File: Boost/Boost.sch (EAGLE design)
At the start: 2 parts

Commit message: boost
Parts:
- added C1: 10nF, adafruit:CPOL-USE2.5-5
- added C2, C4, C5, C6: 22uF, adafruit:CPOL-USE2.5-5
- added JP1: (no value), adafruit:PINHD-1X3
- added JP2: M02PTH, SparkFun-Connectors:M02PTH
- added L1: 1uH, eagle-ltspice:L0207/10
- added R3: 1M Ohm, adafruit:R-US_0207/10
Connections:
- new net N$1: C1.-, C4.-, C6.-, JP1.1, JP2.2, TPS61230.GND
- new net N$10: C2.-, C5.+
- new net N$2: R3.1, TPS61230.PG
- new net N$3: L1.2, TPS61230.SW1, TPS61230.SW2
- new net N$4: C2.+, JP1.3, R3.2, TPS61230.VOUT1, TPS61230.VOUT2
- new net N$5: JP1.2, TPS61230.FB
- new net N$7: C1.+, TPS61230.SS
- new net N$8: C4.+, JP2.1, L1.1, TPS61230.EN, TPS61230.VIN
- new net N$9: C5.-, C6.+

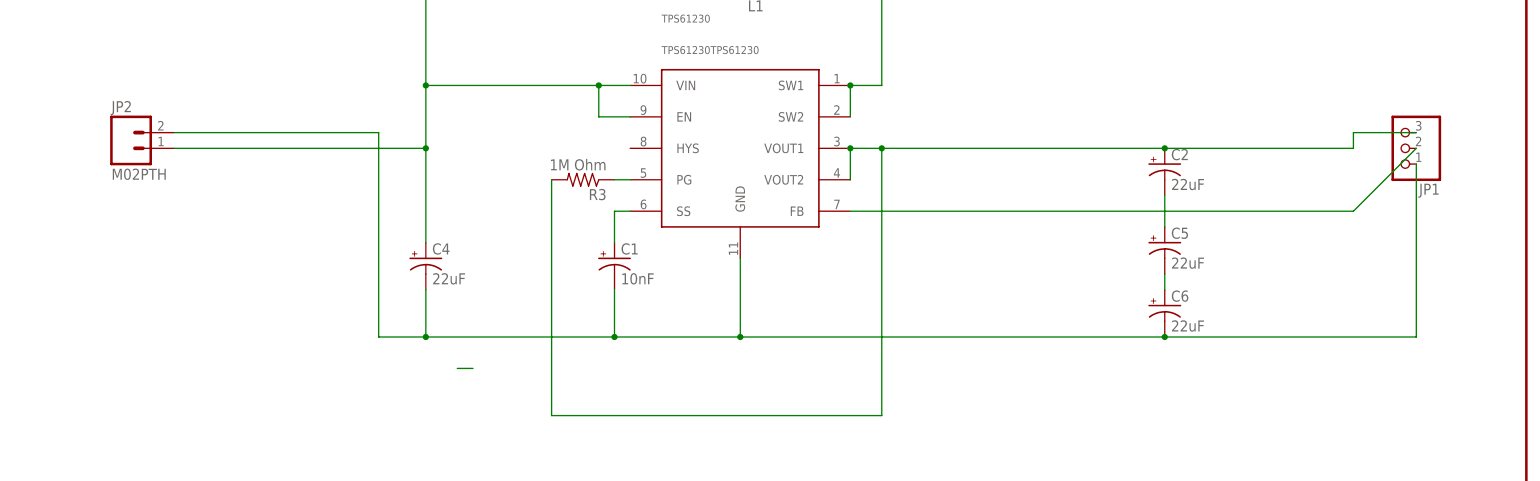
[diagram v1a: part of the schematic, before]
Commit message: Made some changes to feedback loop and reorganized controller
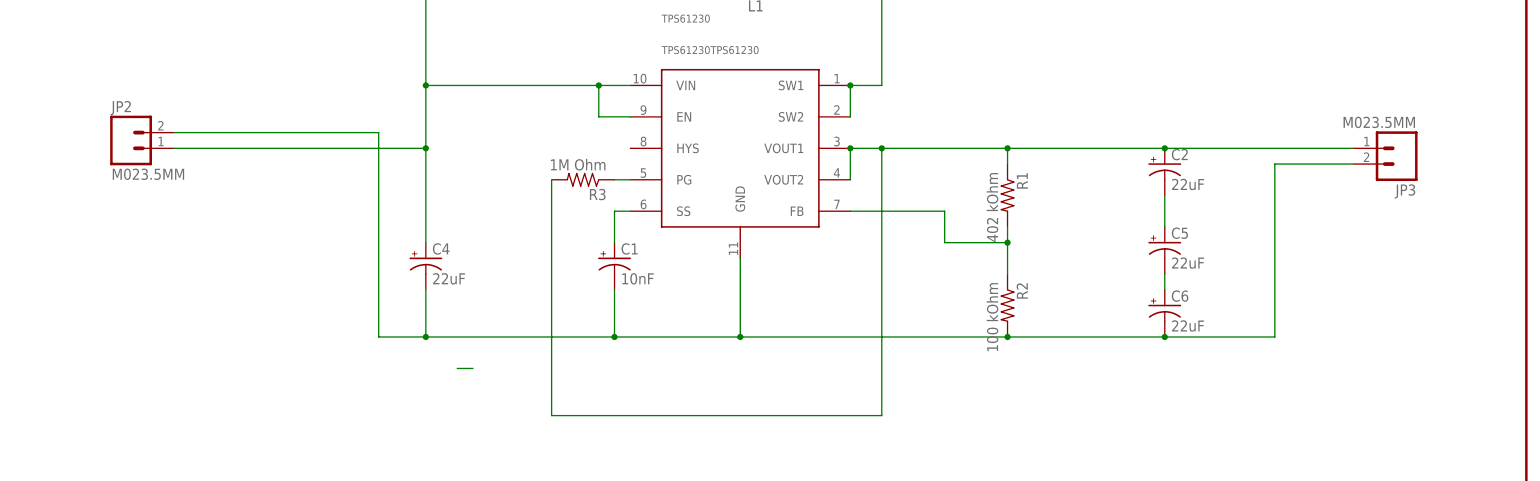
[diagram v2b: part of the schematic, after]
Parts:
- removed JP1: (no value), adafruit:PINHD-1X3
- added JP3: M023.5MM, SparkFun-Connectors:M023.5MM
- added R1: 402 kOhm, adafruit:R-US_0207/10
- added R2: 100 kOhm, adafruit:R-US_0207/10
- JP2: value M02PTH -> M023.5MM; device SparkFun-Connectors:M02PTH -> SparkFun-Connectors:M023.5MM
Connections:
- removed net N$5: JP1.2, TPS61230.FB
- new net N$11: R1.2, R2.1, TPS61230.FB
- net N$1: now also JP3.2, R2.2; no longer JP1.1
- net N$4: now also JP3.1, R1.1; no longer JP1.3
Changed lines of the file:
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@@
 <part name="TPS61230" library="TPS61230" deviceset="TPS61230" device="TPS61230"/>
 <part name="FRAME1" library="SparkFun-Aesthetics" deviceset="FRAME-LETTER" device=""/>
-<part name="JP1" library="adafruit" deviceset="PINHD-1X3" device=""/>
-<part name="JP2" library="SparkFun-Connectors" deviceset="M02" device="PTH"/>
+<part name="JP2" library="SparkFun-Connectors" deviceset="M02" device="3.5MM" value="M023.5MM"/>
 <part name="R3" library="adafruit" deviceset="R-US_" device="0207/10" value="1M Ohm"/>
 <part name="C4" library="adafruit" deviceset="CPOL-US" device="E2.5-5" value="22uF"/>
@@
 <part name="C6" library="adafruit" deviceset="CPOL-US" device="E2.5-5" value="22uF"/>
 <part name="C1" library="adafruit" deviceset="CPOL-US" device="E2.5-5" value="10nF"/>
+<part name="JP3" library="SparkFun-Connectors" deviceset="M02" device="3.5MM" value="M023.5MM"/>
+<part name="R1" library="adafruit" deviceset="R-US_" device="0207/10" value="402 kOhm"/>
+<part name="R2" library="adafruit" deviceset="R-US_" device="0207/10" value="100 kOhm"/>
 </parts>
 <sheets>
@@
 <instance part="FRAME1" gate="G$1" x="0" y="0"/>
 <instance part="FRAME1" gate="G$2" x="147.32" y="0"/>
-<instance part="JP1" gate="A" x="228.6" y="109.22" rot="R180"/>
 <instance part="JP2" gate="G$1" x="22.86" y="109.22"/>
 <instance part="R3" gate="G$1" x="96.52" y="104.14" rot="R180"/>
@@
 <instance part="C6" gate="G$1" x="190.5" y="83.82"/>
 <instance part="C1" gate="G$1" x="101.6" y="91.44"/>
+<instance part="JP3" gate="G$1" x="228.6" y="109.22" rot="R180"/>
+<instance part="R1" gate="G$1" x="165.1" y="101.6" rot="R270"/>
+<instance part="R2" gate="G$1" x="165.1" y="83.82" rot="R270"/>
 </instances>
 <busses>
@@
 <segment>
 <wire x1="63.5" y1="78.74" x2="71.12" y2="78.74" width="0.1524" layer="91"/>
-<pinref part="JP1" gate="A" pin="1"/>
 <wire x1="71.12" y1="78.74" x2="101.6" y2="78.74" width="0.1524" layer="91"/>
 <wire x1="101.6" y1="78.74" x2="121.92" y2="78.74" width="0.1524" layer="91"/>
-<wire x1="121.92" y1="78.74" x2="190.5" y2="78.74" width="0.1524" layer="91"/>
-<wire x1="190.5" y1="78.74" x2="231.14" y2="78.74" width="0.1524" layer="91"/>
-<wire x1="231.14" y1="78.74" x2="231.14" y2="106.68" width="0.1524" layer="91"/>
+<wire x1="121.92" y1="78.74" x2="165.1" y2="78.74" width="0.1524" layer="91"/>
+<wire x1="165.1" y1="78.74" x2="190.5" y2="78.74" width="0.1524" layer="91"/>
 <wire x1="101.6" y1="86.36" x2="101.6" y2="78.74" width="0.1524" layer="91"/>
 <junction x="101.6" y="78.74"/>
@@
 <junction x="121.92" y="78.74"/>
 <pinref part="C6" gate="G$1" pin="-"/>
+<pinref part="C1" gate="G$1" pin="-"/>
+<pinref part="JP3" gate="G$1" pin="2"/>
+<wire x1="220.98" y1="106.68" x2="208.28" y2="106.68" width="0.1524" layer="91"/>
+<wire x1="208.28" y1="106.68" x2="208.28" y2="78.74" width="0.1524" layer="91"/>
+<wire x1="208.28" y1="78.74" x2="190.5" y2="78.74" width="0.1524" layer="91"/>
 <junction x="190.5" y="78.74"/>
-<pinref part="C1" gate="G$1" pin="-"/>
+<pinref part="R2" gate="G$1" pin="2"/>
+<junction x="165.1" y="78.74"/>
 </segment>
 </net>
@@
 <pinref part="TPS61230" gate="G$1" pin="VOUT1"/>
 <wire x1="139.7" y1="109.22" x2="144.78" y2="109.22" width="0.1524" layer="91"/>
-<wire x1="144.78" y1="109.22" x2="190.5" y2="109.22" width="0.1524" layer="91"/>
+<wire x1="144.78" y1="109.22" x2="165.1" y2="109.22" width="0.1524" layer="91"/>
+<wire x1="165.1" y1="109.22" x2="190.5" y2="109.22" width="0.1524" layer="91"/>
 <wire x1="190.5" y1="109.22" x2="220.98" y2="109.22" width="0.1524" layer="91"/>
-<wire x1="220.98" y1="109.22" x2="220.98" y2="111.76" width="0.1524" layer="91"/>
-<wire x1="220.98" y1="111.76" x2="231.14" y2="111.76" width="0.1524" layer="91"/>
-<pinref part="JP1" gate="A" pin="3"/>
 <pinref part="TPS61230" gate="G$1" pin="VOUT2"/>
 <wire x1="139.7" y1="109.22" x2="139.7" y2="104.14" width="0.1524" layer="91"/>
@@
 <pinref part="C2" gate="G$1" pin="+"/>
 <junction x="190.5" y="109.22"/>
-</segment>
-</net>
-<net name="N$5" class="0">
-<segment>
-<pinref part="TPS61230" gate="G$1" pin="FB"/>
-<pinref part="JP1" gate="A" pin="2"/>
-<wire x1="139.7" y1="99.06" x2="220.98" y2="99.06" width="0.1524" layer="91"/>
-<wire x1="220.98" y1="99.06" x2="231.14" y2="109.22" width="0.1524" layer="91"/>
+<pinref part="JP3" gate="G$1" pin="1"/>
+<pinref part="R1" gate="G$1" pin="1"/>
+<wire x1="165.1" y1="109.22" x2="165.1" y2="106.68" width="0.1524" layer="91"/>
+<junction x="165.1" y="109.22"/>
 </segment>
 </net>
@@
 </segment>
 </net>
+<net name="N$11" class="0">
+<segment>
+<pinref part="R1" gate="G$1" pin="2"/>
+<pinref part="R2" gate="G$1" pin="1"/>
+<wire x1="165.1" y1="96.52" x2="165.1" y2="93.98" width="0.1524" layer="91"/>
+<pinref part="TPS61230" gate="G$1" pin="FB"/>
+<wire x1="165.1" y1="93.98" x2="165.1" y2="88.9" width="0.1524" layer="91"/>
+<wire x1="139.7" y1="99.06" x2="154.94" y2="99.06" width="0.1524" layer="91"/>
+<wire x1="154.94" y1="99.06" x2="154.94" y2="93.98" width="0.1524" layer="91"/>
+<wire x1="154.94" y1="93.98" x2="165.1" y2="93.98" width="0.1524" layer="91"/>
+<junction x="165.1" y="93.98"/>
+</segment>
+</net>
